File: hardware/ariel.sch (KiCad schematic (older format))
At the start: 19 parts, among them SW1 SW_Push, U1 WeMos_Battery_Shield, U2 WeMos_D1_mini, U3 74HC595, U4 Si7021_breakout

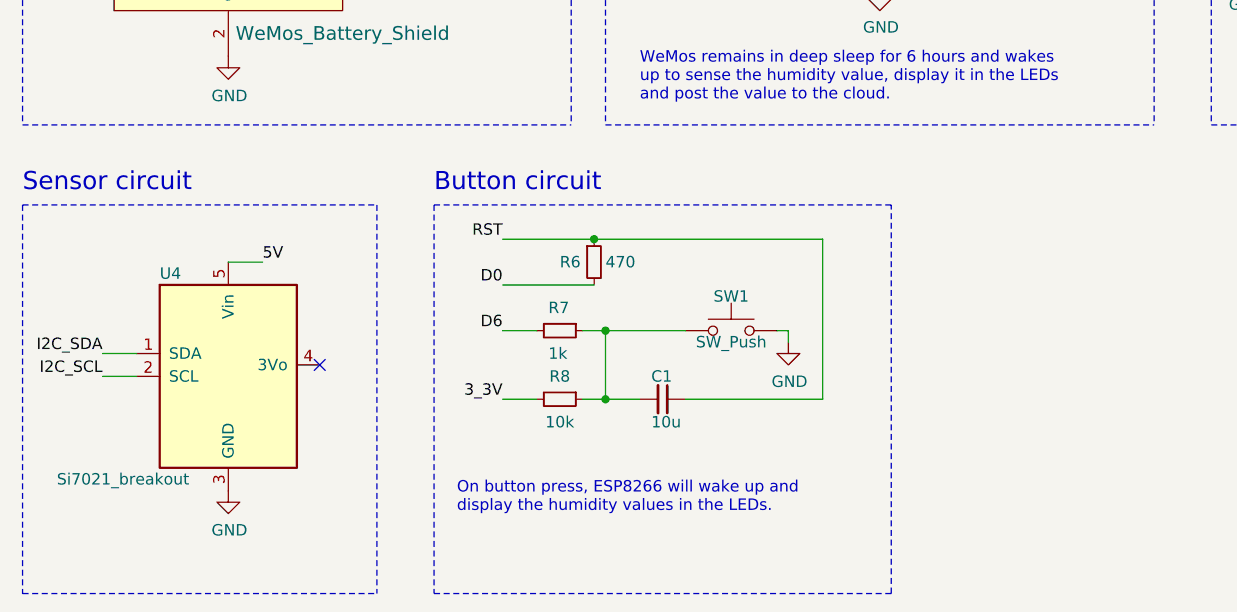
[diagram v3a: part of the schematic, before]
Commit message: Add 0ohm resistor for flexibility of adding breakout boards
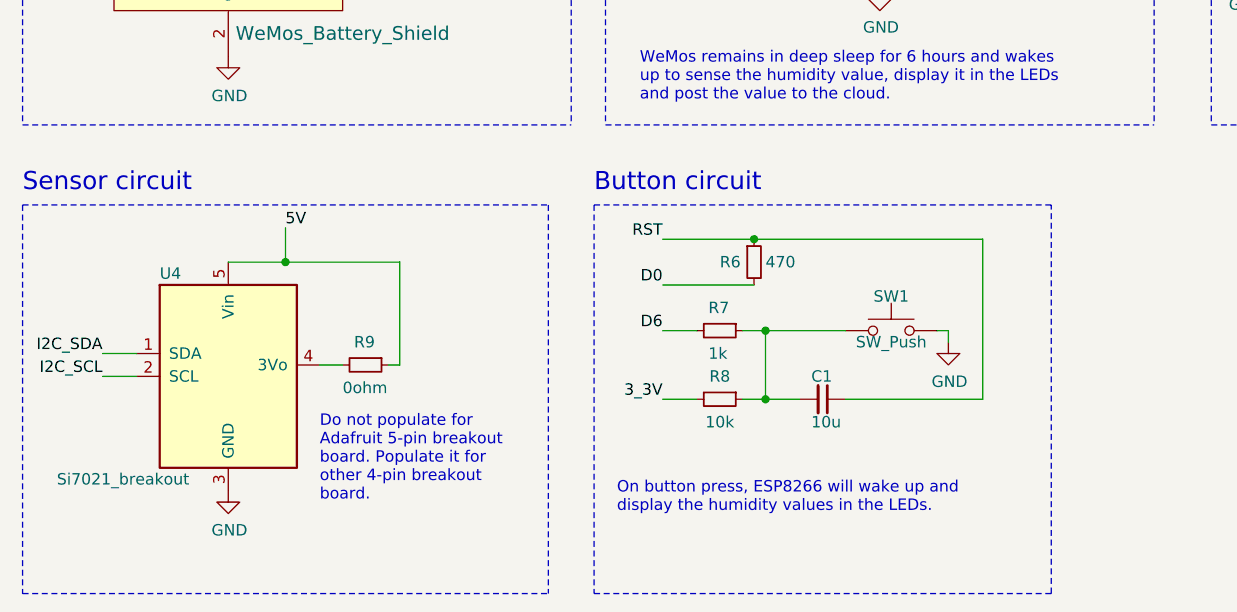
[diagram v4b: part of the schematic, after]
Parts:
- added R9: 0ohm, symbol Device:R_Small
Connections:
- net VCC: now also R9.1
- net at U4.4 (3Vo): now also R9.2
- no-connect marks 21 -> 20
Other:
- note added: "Do not populate for \nAdafruit 5-pin breakout \nboard. Populate it for \nother 4-pin breakout \nboard."
- moved on the sheet: C1, R6, R7, R8, SW1
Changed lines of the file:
@@
 L Device:R_Small R6
 U 1 1 5C7739E8
-P 3400 3600
-F 0 "R6" H 3250 3600 50  0000 L CNN
-F 1 "470" H 3450 3600 50  0000 L CNN
-F 2 "" H 3400 3600 50  0001 C CNN
-F 3 "~" H 3400 3600 50  0001 C CNN
-	1    3400 3600
+P 4100 3600
+F 0 "R6" H 3950 3600 50  0000 L CNN
+F 1 "470" H 4150 3600 50  0000 L CNN
+F 2 "" H 4100 3600 50  0001 C CNN
+F 3 "~" H 4100 3600 50  0001 C CNN
+	1    4100 3600
 	1    0    0    -1
 $EndComp
@@
 L Device:R_Small R7
 U 1 1 5C773C60
-P 3250 3900
-F 0 "R7" V 3150 3850 50  0000 L CNN
-F 1 "1k" V 3350 3850 50  0000 L CNN
-F 2 "" H 3250 3900 50  0001 C CNN
-F 3 "~" H 3250 3900 50  0001 C CNN
-	1    3250 3900
+P 3950 3900
+F 0 "R7" V 3850 3850 50  0000 L CNN
+F 1 "1k" V 4050 3850 50  0000 L CNN
+F 2 "" H 3950 3900 50  0001 C CNN
+F 3 "~" H 3950 3900 50  0001 C CNN
+	1    3950 3900
 	0    1    1    0
 $EndComp
@@
 L Device:R_Small R8
 U 1 1 5C773D83
-P 3250 4200
-F 0 "R8" V 3150 4200 50  0000 C CNN
-F 1 "10k" V 3350 4200 50  0000 C CNN
-F 2 "" H 3250 4200 50  0001 C CNN
-F 3 "~" H 3250 4200 50  0001 C CNN
-	1    3250 4200
+P 3950 4200
+F 0 "R8" V 3850 4200 50  0000 C CNN
+F 1 "10k" V 4050 4200 50  0000 C CNN
+F 2 "" H 3950 4200 50  0001 C CNN
+F 3 "~" H 3950 4200 50  0001 C CNN
+	1    3950 4200
 	0    1    1    0
 $EndComp
@@
 L Device:C_Small C1
 U 1 1 5C773EE5
-P 3700 4200
-F 0 "C1" V 3600 4150 50  0000 L CNN
-F 1 "10u" V 3800 4150 50  0000 L CNN
-F 2 "" H 3700 4200 50  0001 C CNN
-F 3 "~" H 3700 4200 50  0001 C CNN
-	1    3700 4200
+P 4400 4200
+F 0 "C1" V 4300 4150 50  0000 L CNN
+F 1 "10u" V 4500 4150 50  0000 L CNN
+F 2 "" H 4400 4200 50  0001 C CNN
+F 3 "~" H 4400 4200 50  0001 C CNN
+	1    4400 4200
 	0    1    1    0
 $EndComp
@@
 L Switch:SW_Push SW1
 U 1 1 5C85EE0D
-P 4000 3900
-F 0 "SW1" H 4000 4050 50  0000 C CNN
-F 1 "SW_Push" H 4000 3850 50  0000 C CNN
-F 2 "" H 4000 4100 50  0001 C CNN
-F 3 "" H 4000 4100 50  0001 C CNN
-	1    4000 3900
-	1    0    0    -1
-$EndComp
-Wire Wire Line
-	3350 3900 3450 3900
-Wire Wire Line
-	3350 4200 3450 4200
-Wire Wire Line
-	3450 3900 3450 4200
-Connection ~ 3450 3900
-Wire Wire Line
-	3450 3900 3800 3900
-Connection ~ 3450 4200
-Wire Wire Line
-	3450 4200 3600 4200
+P 4700 3900
+F 0 "SW1" H 4700 4050 50  0000 C CNN
+F 1 "SW_Push" H 4700 3850 50  0000 C CNN
+F 2 "" H 4700 4100 50  0001 C CNN
+F 3 "" H 4700 4100 50  0001 C CNN
+	1    4700 3900
+	1    0    0    -1
+$EndComp
+Wire Wire Line
+	4050 3900 4150 3900
+Wire Wire Line
+	4050 4200 4150 4200
+Wire Wire Line
+	4150 3900 4150 4200
+Connection ~ 4150 3900
+Wire Wire Line
+	4150 3900 4500 3900
+Connection ~ 4150 4200
+Wire Wire Line
+	4150 4200 4300 4200
 $Comp
 L power:GND #PWR04
 U 1 1 5C8607DD
-P 4250 3950
-F 0 "#PWR04" H 4250 3700 50  0001 C CNN
-F 1 "GND" H 4255 3777 50  0000 C CNN
-F 2 "" H 4250 3950 50  0001 C CNN
-F 3 "" H 4250 3950 50  0001 C CNN
-	1    4250 3950
-	1    0    0    -1
-$EndComp
-Wire Wire Line
-	4200 3900 4250 3900
-Wire Wire Line
-	4250 3900 4250 3950
-Wire Wire Line
-	3400 3500 4400 3500
-Wire Wire Line
-	4400 3500 4400 4200
-Wire Wire Line
-	4400 4200 3800 4200
+P 4950 3950
+F 0 "#PWR04" H 4950 3700 50  0001 C CNN
+F 1 "GND" H 4955 3777 50  0000 C CNN
+F 2 "" H 4950 3950 50  0001 C CNN
+F 3 "" H 4950 3950 50  0001 C CNN
+	1    4950 3950
+	1    0    0    -1
+$EndComp
+Wire Wire Line
+	4900 3900 4950 3900
+Wire Wire Line
+	4950 3900 4950 3950
+Wire Wire Line
+	4100 3500 5100 3500
+Wire Wire Line
+	5100 3500 5100 4200
+Wire Wire Line
+	5100 4200 4500 4200
 $Comp
 L power:GND #PWR05
@@
 Wire Wire Line
 	2500 1750 2650 1750
-Text Label 3000 3500 2    50   ~ 0
+Text Label 3700 3500 2    50   ~ 0
 RST
-Text Label 3000 3700 2    50   ~ 0
+Text Label 3700 3700 2    50   ~ 0
 D0
 Text Label 5500 1750 0    50   ~ 0
 D6
-Text Label 3000 3900 2    50   ~ 0
+Text Label 3700 3900 2    50   ~ 0
 D6
-Text Label 3000 4200 2    50   ~ 0
+Text Label 3700 4200 2    50   ~ 0
 3_3V
 Wire Wire Line
@@
 WeMos D1 Mini v3.0.0
 Wire Wire Line
-	3400 3500 3000 3500
-Connection ~ 3400 3500
-Wire Wire Line
-	3400 3700 3000 3700
-Wire Wire Line
-	3150 3900 3000 3900
-Wire Wire Line
-	3150 4200 3000 4200
-Wire Notes Line
-	2700 5050 4700 5050
-Wire Notes Line
-	4700 5050 4700 3350
-Wire Notes Line
-	4700 3350 2700 3350
-Wire Notes Line
-	2700 3350 2700 5050
-Text Notes 2700 3300 0    79   ~ 0
+	4100 3500 3700 3500
+Connection ~ 4100 3500
+Wire Wire Line
+	4100 3700 3700 3700
+Wire Wire Line
+	3850 3900 3700 3900
+Wire Wire Line
+	3850 4200 3700 4200
+Wire Notes Line
+	3400 5050 5400 5050
+Wire Notes Line
+	5400 5050 5400 3350
+Wire Notes Line
+	5400 3350 3400 3350
+Wire Notes Line
+	3400 3350 3400 5050
+Text Notes 3400 3300 0    79   ~ 0
 Button circuit
 Wire Wire Line
@@
 Text Notes 900  3300 0    79   ~ 0
 Sensor circuit
-Text Notes 2800 4700 0    50   ~ 0
+Text Notes 3500 4700 0    50   ~ 0
 On button press, ESP8266 will wake up and \ndisplay the humidity values in the LEDs.
 Text Notes 2150 1200 0    50   ~ 0
@@
 Wire Notes Line
 	3450 900  5850 900
-Wire Notes Line
-	2450 3350 2450 5050
-Wire Notes Line
-	900  3350 2450 3350
-Wire Notes Line
-	900  5050 2450 5050
 NoConn ~ 1100 2300
 Wire Notes Line
@@
 Wire Wire Line
 	1400 4100 1250 4100
-Text Label 1950 3600 0    50   ~ 0
+Text Label 2050 3450 0    50   ~ 0
 5V
-Wire Wire Line
-	1800 3600 1950 3600
-NoConn ~ 2200 4050
 Wire Wire Line
 	8850 1850 8950 1850
@@
 Wire Wire Line
 	8450 2350 8450 2550
+Text Label 8950 1850 0    50   ~ 0
+EN
+$Comp
+L Device:R_Small R9
+U 1 1 5C9E0F92
+P 2400 4050
+F 0 "R9" V 2300 4000 50  0000 L CNN
+F 1 "0ohm" V 2500 3950 50  0000 L CNN
+F 2 "" H 2400 4050 50  0001 C CNN
+F 3 "~" H 2400 4050 50  0001 C CNN
+	1    2400 4050
+	0    1    1    0
+$EndComp
+Wire Wire Line
+	2200 4050 2300 4050
+Wire Wire Line
+	2050 3600 2050 3450
+Wire Wire Line
+	1800 3600 2050 3600
+Connection ~ 2050 3600
+Text Notes 2200 4650 0    50   ~ 0
+Do not populate for \nAdafruit 5-pin breakout \nboard. Populate it for \nother 4-pin breakout \nboard.
+Wire Wire Line
+	2550 3600 2550 4050
+Wire Wire Line
+	2550 4050 2500 4050
+Wire Wire Line
+	2050 3600 2550 3600
+Wire Notes Line
+	3200 3350 3200 5050
+Wire Notes Line
+	900  5050 3200 5050
+Wire Notes Line
+	900  3350 3200 3350
+Wire Bus Line
+	7350 1050 7350 2400
 Wire Bus Line
 	7550 1050 7550 1550
-Wire Bus Line
-	7350 1050 7350 2400
-Text Label 8950 1850 0    50   ~ 0
-EN
 $EndSCHEMATC

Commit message: Add mechanical pieces
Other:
- note added: "Do not populate for \nAdafruit 5-pin Si7021 \nbreakout board. \n\nPopulate it for other \n4-pin Si7021 breakout \nboards."
- note removed: "Do not populate for \nAdafruit 5-pin breakout \nboard. Populate it for \nother 4-pin breakout \nboard."
- moved on the sheet: C1, D1, D2, D3, D4, D5, R1, R2, R3, R4, R5, R6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

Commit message: Link symbols to footprint
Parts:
- C1: footprint (none) -> Capacitor_SMD:C_1206_3216Metric
- D1, D2, D3, D4, D5: footprint (none) -> LED_SMD:LED_1206_3216Metric_Pad1.42x1.75mm_HandSolder
- R1, R2, R3, R4, R5, R6, R7, R8, R9: footprint (none) -> Resistor_SMD:R_1206_3216Metric_Pad1.42x1.75mm_HandSolder
- SW1: footprint (none) -> Button_Switch_SMD:SW_SPST_EVPBF
- U1, U2: footprint (none) -> WeMos:D1_mini_board
- U4: footprint (none) -> Connector_PinHeader_2.54mm:PinHeader_1x05_P2.54mm_Vertical
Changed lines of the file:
@@
 F 0 "R6" H 4050 3600 50  0000 L CNN
 F 1 "470" H 4250 3600 50  0000 L CNN
-F 2 "" H 4200 3600 50  0001 C CNN
+F 2 "Resistor_SMD:R_1206_3216Metric_Pad1.42x1.75mm_HandSolder" H 4200 3600 50  0001 C CNN
 F 3 "~" H 4200 3600 50  0001 C CNN
 	1    4200 3600
@@
 F 0 "R7" V 3950 3850 50  0000 L CNN
 F 1 "1k" V 4150 3850 50  0000 L CNN
-F 2 "" H 4050 3900 50  0001 C CNN
+F 2 "Resistor_SMD:R_1206_3216Metric_Pad1.42x1.75mm_HandSolder" H 4050 3900 50  0001 C CNN
 F 3 "~" H 4050 3900 50  0001 C CNN
 	1    4050 3900
@@
 F 0 "R8" V 3950 4200 50  0000 C CNN
 F 1 "10k" V 4150 4200 50  0000 C CNN
-F 2 "" H 4050 4200 50  0001 C CNN
+F 2 "Resistor_SMD:R_1206_3216Metric_Pad1.42x1.75mm_HandSolder" H 4050 4200 50  0001 C CNN
 F 3 "~" H 4050 4200 50  0001 C CNN
 	1    4050 4200
@@
 F 0 "C1" V 4400 4150 50  0000 L CNN
 F 1 "10u" V 4600 4150 50  0000 L CNN
-F 2 "" H 4500 4200 50  0001 C CNN
+F 2 "Capacitor_SMD:C_1206_3216Metric" H 4500 4200 50  0001 C CNN
 F 3 "~" H 4500 4200 50  0001 C CNN
 	1    4500 4200
@@
 F 0 "SW1" H 4800 4050 50  0000 C CNN
 F 1 "SW_Push" H 4800 3850 50  0000 C CNN
-F 2 "" H 4800 4100 50  0001 C CNN
+F 2 "Button_Switch_SMD:SW_SPST_EVPBF" H 4800 4100 50  0001 C CNN
 F 3 "" H 4800 4100 50  0001 C CNN
 	1    4800 3900
@@
 F 0 "D1" H 6950 1200 50  0000 C CNN
 F 1 "LED" H 6950 1000 50  0000 C CNN
-F 2 "" H 6950 1100 50  0001 C CNN
+F 2 "LED_SMD:LED_1206_3216Metric_Pad1.42x1.75mm_HandSolder" H 6950 1100 50  0001 C CNN
 F 3 "~" H 6950 1100 50  0001 C CNN
 	1    6950 1100
@@
 F 0 "D2" H 6950 1500 50  0000 C CNN
 F 1 "LED" H 6950 1300 50  0000 C CNN
-F 2 "" H 6950 1400 50  0001 C CNN
+F 2 "LED_SMD:LED_1206_3216Metric_Pad1.42x1.75mm_HandSolder" H 6950 1400 50  0001 C CNN
 F 3 "~" H 6950 1400 50  0001 C CNN
 	1    6950 1400
@@
 F 0 "D3" H 6950 1800 50  0000 C CNN
 F 1 "LED" H 6950 1600 50  0000 C CNN
-F 2 "" H 6950 1700 50  0001 C CNN
+F 2 "LED_SMD:LED_1206_3216Metric_Pad1.42x1.75mm_HandSolder" H 6950 1700 50  0001 C CNN
 F 3 "~" H 6950 1700 50  0001 C CNN
 	1    6950 1700
@@
 F 0 "D4" H 6950 2100 50  0000 C CNN
 F 1 "LED" H 6950 1900 50  0000 C CNN
-F 2 "" H 6950 2000 50  0001 C CNN
+F 2 "LED_SMD:LED_1206_3216Metric_Pad1.42x1.75mm_HandSolder" H 6950 2000 50  0001 C CNN
 F 3 "~" H 6950 2000 50  0001 C CNN
 	1    6950 2000
@@
 F 0 "D5" H 6950 2400 50  0000 C CNN
 F 1 "LED" H 6950 2200 50  0000 C CNN
-F 2 "" H 6950 2300 50  0001 C CNN
+F 2 "LED_SMD:LED_1206_3216Metric_Pad1.42x1.75mm_HandSolder" H 6950 2300 50  0001 C CNN
 F 3 "~" H 6950 2300 50  0001 C CNN
 	1    6950 2300
@@
 F 0 "R1" V 7100 1050 50  0000 L CNN
 F 1 "1k" V 7300 1050 50  0000 L CNN
-F 2 "" H 7200 1100 50  0001 C CNN
+F 2 "Resistor_SMD:R_1206_3216Metric_Pad1.42x1.75mm_HandSolder" H 7200 1100 50  0001 C CNN
 F 3 "~" H 7200 1100 50  0001 C CNN
 	1    7200 1100
@@
 F 0 "R2" V 7100 1350 50  0000 L CNN
 F 1 "1k" V 7300 1350 50  0000 L CNN
-F 2 "" H 7200 1400 50  0001 C CNN
+F 2 "Resistor_SMD:R_1206_3216Metric_Pad1.42x1.75mm_HandSolder" H 7200 1400 50  0001 C CNN
 F 3 "~" H 7200 1400 50  0001 C CNN
 	1    7200 1400
@@
 F 0 "R3" V 7100 1650 50  0000 L CNN
 F 1 "1k" V 7300 1650 50  0000 L CNN
-F 2 "" H 7200 1700 50  0001 C CNN
+F 2 "Resistor_SMD:R_1206_3216Metric_Pad1.42x1.75mm_HandSolder" H 7200 1700 50  0001 C CNN
 F 3 "~" H 7200 1700 50  0001 C CNN
 	1    7200 1700
@@
 F 0 "R4" V 7100 1950 50  0000 L CNN
 F 1 "1k" V 7300 1950 50  0000 L CNN
-F 2 "" H 7200 2000 50  0001 C CNN
+F 2 "Resistor_SMD:R_1206_3216Metric_Pad1.42x1.75mm_HandSolder" H 7200 2000 50  0001 C CNN
 F 3 "~" H 7200 2000 50  0001 C CNN
 	1    7200 2000
@@
 F 0 "R5" V 7100 2250 50  0000 L CNN
 F 1 "1k" V 7300 2250 50  0000 L CNN
-F 2 "" H 7200 2300 50  0001 C CNN
+F 2 "Resistor_SMD:R_1206_3216Metric_Pad1.42x1.75mm_HandSolder" H 7200 2300 50  0001 C CNN
 F 3 "~" H 7200 2300 50  0001 C CNN
 	1    7200 2300
@@
 F 0 "U2" H 5250 2250 60  0000 C CNN
 F 1 "WeMos_D1_mini" H 5200 1100 60  0000 C CNN
-F 2 "" H 5200 1000 60  0000 C CNN
+F 2 "WeMos:D1_mini_board" H 5200 1000 60  0001 C CNN
 F 3 "http://www.wemos.cc/Products/d1_mini.html" H 4800 2494 60  0001 C CNN
 	1    4800 1700
@@
 F 0 "U1" H 2200 2550 60  0000 C CNN
 F 1 "WeMos_Battery_Shield" H 2300 1400 60  0000 C CNN
-F 2 "" H 2200 1300 60  0000 C CNN
+F 2 "WeMos:D1_mini_board" H 2200 1300 60  0001 C CNN
 F 3 "http://www.wemos.cc/Products/d1_mini.html" H 1800 2794 60  0001 C CNN
 	1    1800 2000
@@
 F 0 "U4" H 1500 4550 50  0000 L CNN
 F 1 "Si7021_breakout" H 1050 3650 50  0000 L CNN
-F 2 "" H 1800 3500 50  0000 C CNN
+F 2 "Connector_PinHeader_2.54mm:PinHeader_1x05_P2.54mm_Vertical" H 1800 3500 50  0001 C CNN
 F 3 "https://learn.adafruit.com/adafruit-si7021-temperature-plus-humidity-sensor/downloads" H 1800 3900 50  0001 C CNN
 	1    1800 4100
@@
 F 0 "R9" V 2300 4000 50  0000 L CNN
 F 1 "0ohm" V 2500 3950 50  0000 L CNN
-F 2 "" H 2400 4050 50  0001 C CNN
+F 2 "Resistor_SMD:R_1206_3216Metric_Pad1.42x1.75mm_HandSolder" H 2400 4050 50  0001 C CNN
 F 3 "~" H 2400 4050 50  0001 C CNN
 	1    2400 4050

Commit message: Add BOM notes
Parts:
- U3: footprint (none) -> Package_SO:SOIC-16_3.9x9.9mm_P1.27mm
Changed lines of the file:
@@
 F 0 "U3" H 8450 2200 50  0000 C CNN
 F 1 "74HC595" H 8450 1000 50  0000 C CNN
-F 2 "" H 8650 1650 50  0001 C CNN
+F 2 "Package_SO:SOIC-16_3.9x9.9mm_P1.27mm" H 8650 1650 50  0001 C CNN
 F 3 "http://www.ti.com/lit/ds/symlink/sn74hc595.pdf" H 8650 1650 50  0001 C CNN
 	1    8650 1650

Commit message: Generate net list wirh 0805 instead of 1206
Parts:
- C1: footprint Capacitor_SMD:C_1206_3216Metric -> Capacitor_SMD:C_0805_2012Metric_Pad1.15x1.40mm_HandSolder
- D1, D2, D3, D4, D5: footprint LED_SMD:LED_1206_3216Metric_Pad1.42x1.75mm_HandSolder -> LED_SMD:LED_0805_2012Metric_Pad1.15x1.40mm_HandSolder
- R1, R2, R3, R4, R5, R6, R7, R8, R9: footprint Resistor_SMD:R_1206_3216Metric_Pad1.42x1.75mm_HandSolder -> Resistor_SMD:R_0805_2012Metric_Pad1.15x1.40mm_HandSolder
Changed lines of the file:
@@
 F 0 "R6" H 4050 3600 50  0000 L CNN
 F 1 "470" H 4250 3600 50  0000 L CNN
-F 2 "Resistor_SMD:R_1206_3216Metric_Pad1.42x1.75mm_HandSolder" H 4200 3600 50  0001 C CNN
+F 2 "Resistor_SMD:R_0805_2012Metric_Pad1.15x1.40mm_HandSolder" H 4200 3600 50  0001 C CNN
 F 3 "~" H 4200 3600 50  0001 C CNN
 	1    4200 3600
@@
 F 0 "R7" V 3950 3850 50  0000 L CNN
 F 1 "1k" V 4150 3850 50  0000 L CNN
-F 2 "Resistor_SMD:R_1206_3216Metric_Pad1.42x1.75mm_HandSolder" H 4050 3900 50  0001 C CNN
+F 2 "Resistor_SMD:R_0805_2012Metric_Pad1.15x1.40mm_HandSolder" H 4050 3900 50  0001 C CNN
 F 3 "~" H 4050 3900 50  0001 C CNN
 	1    4050 3900
@@
 F 0 "R8" V 3950 4200 50  0000 C CNN
 F 1 "10k" V 4150 4200 50  0000 C CNN
-F 2 "Resistor_SMD:R_1206_3216Metric_Pad1.42x1.75mm_HandSolder" H 4050 4200 50  0001 C CNN
+F 2 "Resistor_SMD:R_0805_2012Metric_Pad1.15x1.40mm_HandSolder" H 4050 4200 50  0001 C CNN
 F 3 "~" H 4050 4200 50  0001 C CNN
 	1    4050 4200
@@
 F 0 "C1" V 4400 4150 50  0000 L CNN
 F 1 "10u" V 4600 4150 50  0000 L CNN
-F 2 "Capacitor_SMD:C_1206_3216Metric" H 4500 4200 50  0001 C CNN
+F 2 "Capacitor_SMD:C_0805_2012Metric_Pad1.15x1.40mm_HandSolder" H 4500 4200 50  0001 C CNN
 F 3 "~" H 4500 4200 50  0001 C CNN
 	1    4500 4200
@@
 F 0 "D1" H 6950 1200 50  0000 C CNN
 F 1 "LED" H 6950 1000 50  0000 C CNN
-F 2 "LED_SMD:LED_1206_3216Metric_Pad1.42x1.75mm_HandSolder" H 6950 1100 50  0001 C CNN
+F 2 "LED_SMD:LED_0805_2012Metric_Pad1.15x1.40mm_HandSolder" H 6950 1100 50  0001 C CNN
 F 3 "~" H 6950 1100 50  0001 C CNN
 	1    6950 1100
@@
 F 0 "D2" H 6950 1500 50  0000 C CNN
 F 1 "LED" H 6950 1300 50  0000 C CNN
-F 2 "LED_SMD:LED_1206_3216Metric_Pad1.42x1.75mm_HandSolder" H 6950 1400 50  0001 C CNN
+F 2 "LED_SMD:LED_0805_2012Metric_Pad1.15x1.40mm_HandSolder" H 6950 1400 50  0001 C CNN
 F 3 "~" H 6950 1400 50  0001 C CNN
 	1    6950 1400
@@
 F 0 "D3" H 6950 1800 50  0000 C CNN
 F 1 "LED" H 6950 1600 50  0000 C CNN
-F 2 "LED_SMD:LED_1206_3216Metric_Pad1.42x1.75mm_HandSolder" H 6950 1700 50  0001 C CNN
+F 2 "LED_SMD:LED_0805_2012Metric_Pad1.15x1.40mm_HandSolder" H 6950 1700 50  0001 C CNN
 F 3 "~" H 6950 1700 50  0001 C CNN
 	1    6950 1700
@@
 F 0 "D4" H 6950 2100 50  0000 C CNN
 F 1 "LED" H 6950 1900 50  0000 C CNN
-F 2 "LED_SMD:LED_1206_3216Metric_Pad1.42x1.75mm_HandSolder" H 6950 2000 50  0001 C CNN
+F 2 "LED_SMD:LED_0805_2012Metric_Pad1.15x1.40mm_HandSolder" H 6950 2000 50  0001 C CNN
 F 3 "~" H 6950 2000 50  0001 C CNN
 	1    6950 2000
@@
 F 0 "D5" H 6950 2400 50  0000 C CNN
 F 1 "LED" H 6950 2200 50  0000 C CNN
-F 2 "LED_SMD:LED_1206_3216Metric_Pad1.42x1.75mm_HandSolder" H 6950 2300 50  0001 C CNN
+F 2 "LED_SMD:LED_0805_2012Metric_Pad1.15x1.40mm_HandSolder" H 6950 2300 50  0001 C CNN
 F 3 "~" H 6950 2300 50  0001 C CNN
 	1    6950 2300
@@
 F 0 "R1" V 7100 1050 50  0000 L CNN
 F 1 "1k" V 7300 1050 50  0000 L CNN
-F 2 "Resistor_SMD:R_1206_3216Metric_Pad1.42x1.75mm_HandSolder" H 7200 1100 50  0001 C CNN
+F 2 "Resistor_SMD:R_0805_2012Metric_Pad1.15x1.40mm_HandSolder" H 7200 1100 50  0001 C CNN
 F 3 "~" H 7200 1100 50  0001 C CNN
 	1    7200 1100
@@
 F 0 "R2" V 7100 1350 50  0000 L CNN
 F 1 "1k" V 7300 1350 50  0000 L CNN
-F 2 "Resistor_SMD:R_1206_3216Metric_Pad1.42x1.75mm_HandSolder" H 7200 1400 50  0001 C CNN
+F 2 "Resistor_SMD:R_0805_2012Metric_Pad1.15x1.40mm_HandSolder" H 7200 1400 50  0001 C CNN
 F 3 "~" H 7200 1400 50  0001 C CNN
 	1    7200 1400
@@
 F 0 "R3" V 7100 1650 50  0000 L CNN
 F 1 "1k" V 7300 1650 50  0000 L CNN
-F 2 "Resistor_SMD:R_1206_3216Metric_Pad1.42x1.75mm_HandSolder" H 7200 1700 50  0001 C CNN
+F 2 "Resistor_SMD:R_0805_2012Metric_Pad1.15x1.40mm_HandSolder" H 7200 1700 50  0001 C CNN
 F 3 "~" H 7200 1700 50  0001 C CNN
 	1    7200 1700
@@
 F 0 "R4" V 7100 1950 50  0000 L CNN
 F 1 "1k" V 7300 1950 50  0000 L CNN
-F 2 "Resistor_SMD:R_1206_3216Metric_Pad1.42x1.75mm_HandSolder" H 7200 2000 50  0001 C CNN
+F 2 "Resistor_SMD:R_0805_2012Metric_Pad1.15x1.40mm_HandSolder" H 7200 2000 50  0001 C CNN
 F 3 "~" H 7200 2000 50  0001 C CNN
 	1    7200 2000
@@
 F 0 "R5" V 7100 2250 50  0000 L CNN
 F 1 "1k" V 7300 2250 50  0000 L CNN
-F 2 "Resistor_SMD:R_1206_3216Metric_Pad1.42x1.75mm_HandSolder" H 7200 2300 50  0001 C CNN
+F 2 "Resistor_SMD:R_0805_2012Metric_Pad1.15x1.40mm_HandSolder" H 7200 2300 50  0001 C CNN
 F 3 "~" H 7200 2300 50  0001 C CNN
 	1    7200 2300
@@
 F 0 "R9" V 2300 4000 50  0000 L CNN
 F 1 "0ohm" V 2500 3950 50  0000 L CNN
-F 2 "Resistor_SMD:R_1206_3216Metric_Pad1.42x1.75mm_HandSolder" H 2400 4050 50  0001 C CNN
+F 2 "Resistor_SMD:R_0805_2012Metric_Pad1.15x1.40mm_HandSolder" H 2400 4050 50  0001 C CNN
 F 3 "~" H 2400 4050 50  0001 C CNN
 	1    2400 4050
